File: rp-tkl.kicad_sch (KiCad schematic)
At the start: 33 parts, among them J1 USB_C_Receptacle_USB2.0, J2 SWD, SW0 SW_Push, U1 XC6206PxxxMR, U2 RP2040, U3 SRV05-4, U4 W25Q128JVS, Y1 12MHz

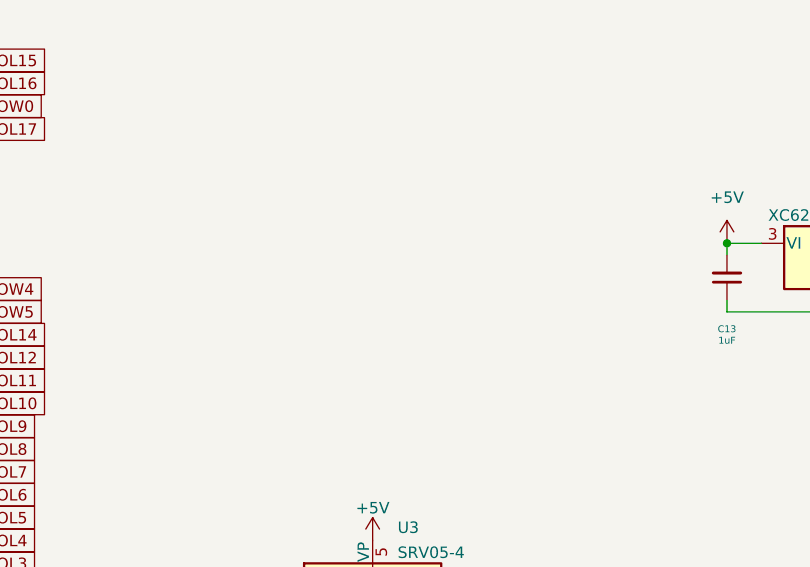
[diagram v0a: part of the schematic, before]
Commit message: Added JST Connector
Also cleaned up everything, 99% done
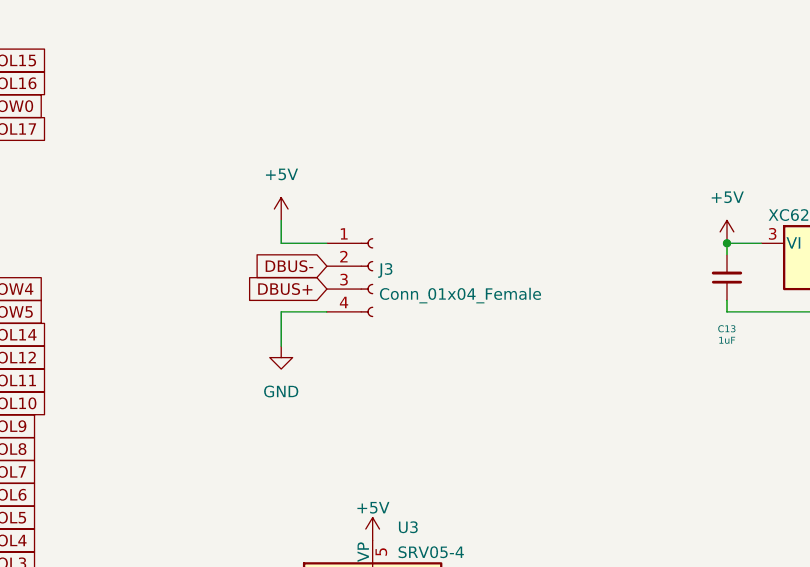
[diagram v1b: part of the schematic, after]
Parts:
- added J3: Conn_01x04_Female, Connector_JST:JST_SH_SM04B-SRSS-TB_1x04-1MP_P1.00mm_Horizontal, symbol Connector:Conn_01x04_Female
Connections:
- net +5V: now also J3.1 (Pin_1)
- net DBUS+: now also J3.3 (Pin_3)
- net DBUS-: now also J3.2 (Pin_2)
- net GND: now also J3.4 (Pin_4)
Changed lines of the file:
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@@
   (no_connect (at 72.39 199.39))
   (no_connect (at 72.39 201.93))
+  (wire (pts (xy 125.73 69.85) (xy 120.65 69.85))
+    (stroke (width 0) (type default) (color 0 0 0 0))
+  )
   (wire (pts (xy 87.63 171.45) (xy 92.71 171.45))
     (stroke (width 0) (type default) (color 0 0 0 0))
   )
+  (wire (pts (xy 125.73 77.47) (xy 120.65 77.47))
+    (stroke (width 0) (type default) (color 0 0 0 0))
+  )
   (wire (pts (xy 281.305 68.58) (xy 281.305 69.85))
     (stroke (width 0) (type default) (color 0 0 0 0))
@@
   )
   (wire (pts (xy 176.53 118.11) (xy 182.88 118.11))
+    (stroke (width 0) (type default) (color 0 0 0 0))
+  )
+  (wire (pts (xy 120.65 77.47) (xy 120.65 81.28))
     (stroke (width 0) (type default) (color 0 0 0 0))
   )
@@
   (wire (pts (xy 189.23 69.85) (xy 193.04 69.85))
     (stroke (width 0) (type solid) (color 0 0 0 0))
+  )
+  (wire (pts (xy 120.65 67.31) (xy 120.65 69.85))
+    (stroke (width 0) (type default) (color 0 0 0 0))
   )
   (wire (pts (xy 213.36 76.2) (xy 217.17 76.2))
@@
     )
   )
+  (global_label "DBUS+" (shape input) (at 125.73 74.93 180) (fields_autoplaced)
+    (effects (font (size 1.27 1.27)) (justify right))
+    (property "Intersheet References" "${INTERSHEET_REFS}" (id 0) (at 116.6645 74.8506 0)
+      (effects (font (size 1.27 1.27)) (justify right) hide)
+    )
+  )
   (global_label "DBUS-" (shape input) (at 143.51 118.11 0) (fields_autoplaced)
     (effects (font (size 1.27 1.27)) (justify left))
@@
     )
   )
+  (global_label "DBUS-" (shape input) (at 125.73 72.39 180) (fields_autoplaced)
+    (effects (font (size 1.27 1.27)) (justify right))
+    (property "Intersheet References" "${INTERSHEET_REFS}" (id 0) (at 116.6645 72.3106 0)
+      (effects (font (size 1.27 1.27)) (justify right) hide)
+    )
+  )
   (global_label "~{RESET}" (shape input) (at 240.03 111.76 0) (fields_autoplaced)
     (effects (font (size 1.27 1.27)) (justify left))
@@
     (pin "5")
     (pin "6")
+  )
+  (symbol (lib_id "power:GND") (at 120.65 81.28 0) (unit 1)
+    (in_bom yes) (on_board yes) (fields_autoplaced)
+    (property "Reference" "#PWR029" (id 0) (at 120.65 87.63 0)
+      (effects (font (size 1.27 1.27)) hide)
+    )
+    (property "Value" "GND" (id 1) (at 120.65 86.36 0))
+    (property "Footprint" "" (id 2) (at 120.65 81.28 0)
+      (effects (font (size 1.27 1.27)) hide)
+    )
+    (property "Datasheet" "" (id 3) (at 120.65 81.28 0)
+      (effects (font (size 1.27 1.27)) hide)
+    )
+    (pin "1")
   )
   (symbol (lib_id "Device:R_Small") (at 195.58 118.11 90) (unit 1)
@@
     (pin "1")
   )
+  (symbol (lib_id "power:+5V") (at 120.65 67.31 0) (unit 1)
+    (in_bom yes) (on_board yes) (fields_autoplaced)
+    (property "Reference" "#PWR0103" (id 0) (at 120.65 71.12 0)
+      (effects (font (size 1.27 1.27)) hide)
+    )
+    (property "Value" "+5V" (id 1) (at 120.65 62.23 0))
+    (property "Footprint" "" (id 2) (at 120.65 67.31 0)
+      (effects (font (size 1.27 1.27)) hide)
+    )
+    (property "Datasheet" "" (id 3) (at 120.65 67.31 0)
+      (effects (font (size 1.27 1.27)) hide)
+    )
+    (pin "1")
+  )
   (symbol (lib_id "Device:Crystal_GND24_Small") (at 182.88 115.57 90) (unit 1)
     (in_bom yes) (on_board yes)
@@
     (pin "1")
   )
+  (symbol (lib_id "Connector:Conn_01x04_Female") (at 130.81 72.39 0) (unit 1)
+    (in_bom yes) (on_board yes) (fields_autoplaced)
+    (property "Reference" "J3" (id 0) (at 131.5212 72.7515 0)
+      (effects (font (size 1.27 1.27)) (justify left))
+    )
+    (property "Value" "Conn_01x04_Female" (id 1) (at 131.5212 75.5266 0)
+      (effects (font (size 1.27 1.27)) (justify left))
+    )
+    (property "Footprint" "Connector_JST:JST_SH_SM04B-SRSS-TB_1x04-1MP_P1.00mm_Horizontal" (id 2) (at 130.81 72.39 0)
+      (effects (font (size 1.27 1.27)) hide)
+    )
+    (property "Datasheet" "~" (id 3) (at 130.81 72.39 0)
+      (effects (font (size 1.27 1.27)) hide)
+    )
+    (pin "1")
+    (pin "2")
+    (pin "3")
+    (pin "4")
+  )
   (symbol (lib_id "Device:C_Small") (at 222.25 72.39 0) (unit 1)
     (in_bom yes) (on_board yes)
@@
       (reference "#PWR027") (unit 1) (value "GND") (footprint "")
     )
+    (path "/40aa9167-fdb5-46eb-9a4f-8c98d55681c9"
+      (reference "#PWR029") (unit 1) (value "GND") (footprint "")
+    )
     (path "/13bc3998-5745-424e-ada9-f8a9e1f5329c"
       (reference "#PWR0101") (unit 1) (value "+3V3") (footprint "")
@@
       (reference "#PWR0102") (unit 1) (value "+1V1") (footprint "")
     )
+    (path "/79db240d-9612-4f89-9692-5a027e4d42fe"
+      (reference "#PWR0103") (unit 1) (value "+5V") (footprint "")
+    )
     (path "/29f11a32-f398-46d6-95a0-57f3be58392e"
       (reference "C1") (unit 1) (value "1uF") (footprint "Capacitor_SMD:C_0402_1005Metric")
@@
       (reference "J2") (unit 1) (value "SWD") (footprint "Connector_PinSocket_2.54mm:PinSocket_1x05_P2.54mm_Vertical")
     )
+    (path "/cd299587-3566-48c2-b7b0-ede206393480"
+      (reference "J3") (unit 1) (value "Conn_01x04_Female") (footprint "Connector_JST:JST_SH_SM04B-SRSS-TB_1x04-1MP_P1.00mm_Horizontal")
+    )
     (path "/d5f64c48-5769-4554-8a1d-d23f7b2152b1"

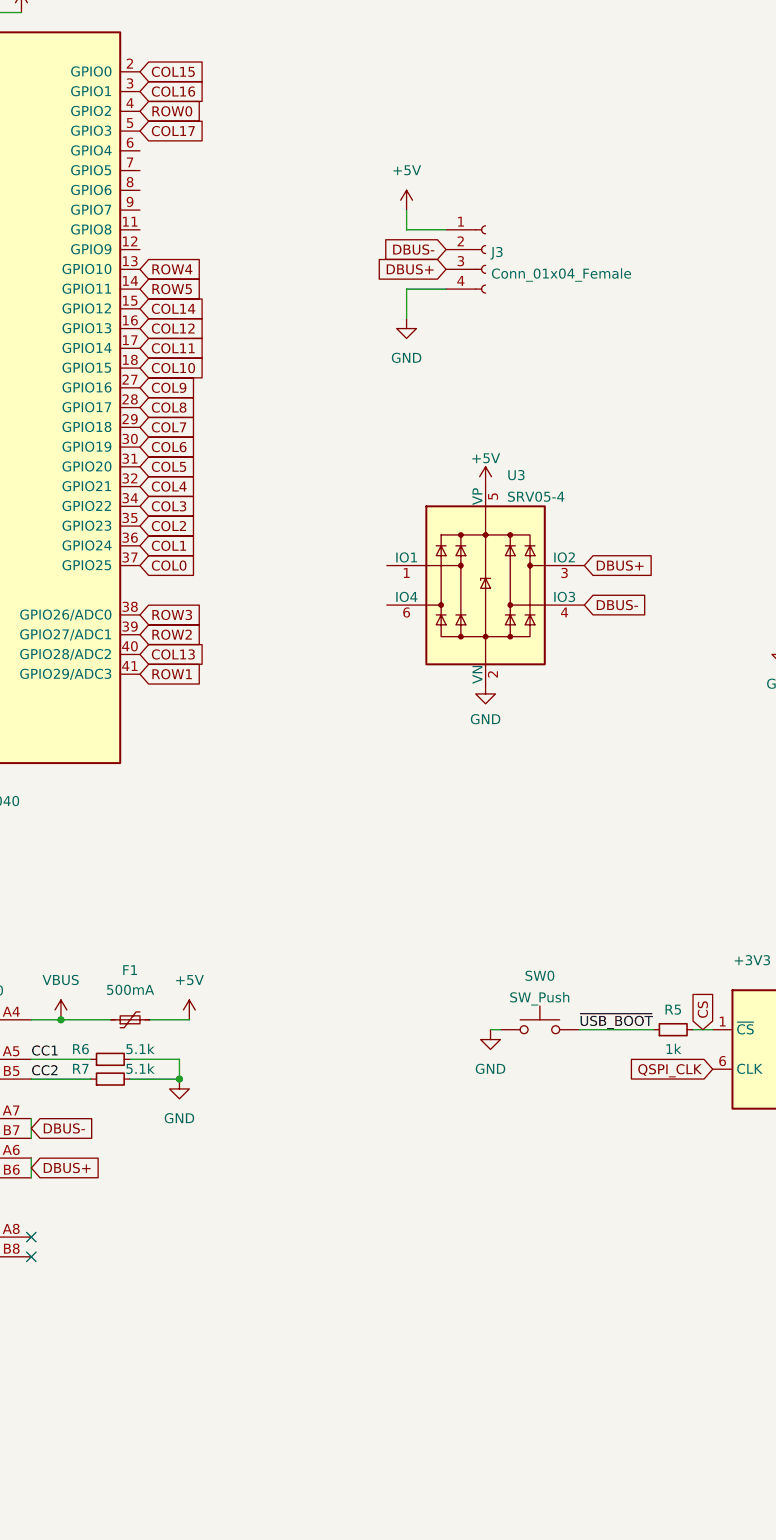
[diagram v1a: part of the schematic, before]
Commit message: More cleanup, added connector for/broke out unused pins
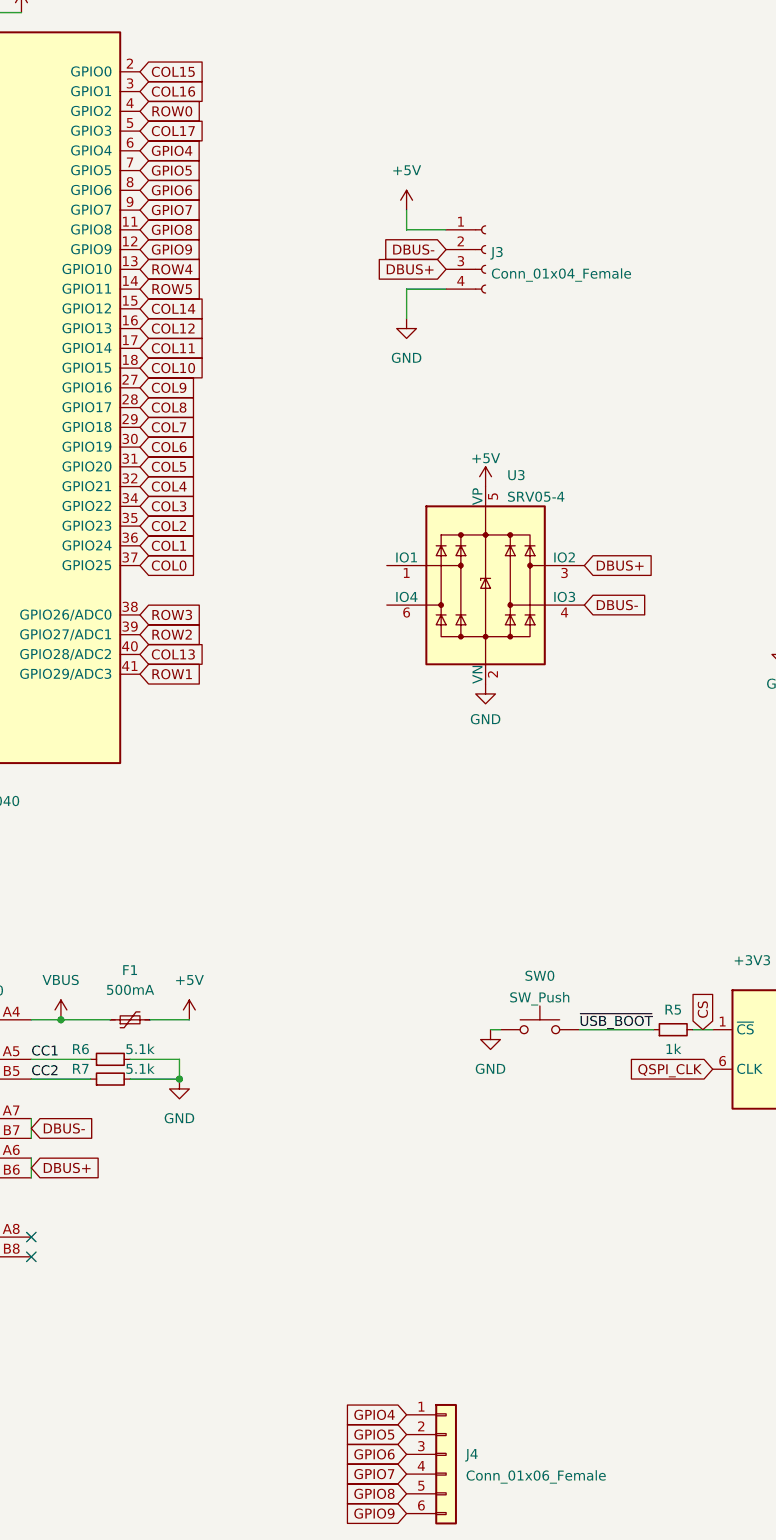
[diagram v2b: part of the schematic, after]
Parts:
- added J4: Conn_01x06_Female, Connector_PinSocket_2.54mm:PinSocket_1x06_P2.54mm_Vertical, symbol Connector_Generic:Conn_01x06
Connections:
- net GPIO8: now reaches U2.11 (GPIO8)
- net GPIO8: now also J4.5 (Pin_5)
- net GPIO9: now reaches U2.12 (GPIO9)
- net GPIO9: now also J4.6 (Pin_6)
- net GPIO4: now reaches U2.6 (GPIO4)
- net GPIO4: now also J4.1 (Pin_1)
- net GPIO5: now reaches U2.7 (GPIO5)
- net GPIO5: now also J4.2 (Pin_2)
- net GPIO6: now reaches U2.8 (GPIO6)
- net GPIO6: now also J4.3 (Pin_3)
- net GPIO7: now reaches U2.9 (GPIO7)
- net GPIO7: now also J4.4 (Pin_4)
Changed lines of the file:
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@@
+    )
+  )
+  (global_label "GPIO4" (shape input) (at 120.65 222.25 180) (fields_autoplaced)
+    (effects (font (size 1.27 1.27)) (justify right))
+    (property "Intersheet References" "${INTERSHEET_REFS}" (id 0) (at 112.5521 222.1706 0)
+      (effects (font (size 1.27 1.27)) (justify right) hide)
     )
   )
@@
     )
   )
+  (global_label "GPIO6" (shape input) (at 120.65 227.33 180) (fields_autoplaced)
+    (effects (font (size 1.27 1.27)) (justify right))
+    (property "Intersheet References" "${INTERSHEET_REFS}" (id 0) (at 112.5521 227.2506 0)
+      (effects (font (size 1.27 1.27)) (justify right) hide)
+    )
+  )
+  (global_label "GPIO7" (shape input) (at 120.65 229.87 180) (fields_autoplaced)
+    (effects (font (size 1.27 1.27)) (justify right))
+    (property "Intersheet References" "${INTERSHEET_REFS}" (id 0) (at 112.5521 229.7906 0)
+      (effects (font (size 1.27 1.27)) (justify right) hide)
+    )
+  )
   (global_label "COL12" (shape input) (at 86.36 82.55 0) (fields_autoplaced)
     (effects (font (size 1.27 1.27)) (justify left))
@@
     )
   )
+  (global_label "GPIO8" (shape input) (at 86.36 69.85 0) (fields_autoplaced)
+    (effects (font (size 1.27 1.27)) (justify left))
+    (property "Intersheet References" "${INTERSHEET_REFS}" (id 0) (at 94.4579 69.7706 0)
+      (effects (font (size 1.27 1.27)) (justify left) hide)
+    )
+  )
   (global_label "SD0" (shape input) (at 185.42 170.18 0) (fields_autoplaced)
     (effects (font (size 1.27 1.27)) (justify left))
@@
     )
   )
+  (global_label "GPIO9" (shape input) (at 120.65 234.95 180) (fields_autoplaced)
+    (effects (font (size 1.27 1.27)) (justify right))
+    (property "Intersheet References" "${INTERSHEET_REFS}" (id 0) (at 112.5521 234.8706 0)
+      (effects (font (size 1.27 1.27)) (justify right) hide)
+    )
+  )
+  (global_label "GPIO5" (shape input) (at 120.65 224.79 180) (fields_autoplaced)
+    (effects (font (size 1.27 1.27)) (justify right))
+    (property "Intersheet References" "${INTERSHEET_REFS}" (id 0) (at 112.5521 224.7106 0)
+      (effects (font (size 1.27 1.27)) (justify right) hide)
+    )
+  )
   (global_label "COL0" (shape input) (at 86.36 113.03 0) (fields_autoplaced)
     (effects (font (size 1.27 1.27)) (justify left))
@@
     )
   )
+  (global_label "GPIO4" (shape input) (at 86.36 59.69 0) (fields_autoplaced)
+    (effects (font (size 1.27 1.27)) (justify left))
+    (property "Intersheet References" "${INTERSHEET_REFS}" (id 0) (at 94.4579 59.6106 0)
+      (effects (font (size 1.27 1.27)) (justify left) hide)
+    )
+  )
   (global_label "SD2" (shape input) (at 45.72 121.92 180) (fields_autoplaced)
     (effects (font (size 1.27 1.27)) (justify right))
@@
     )
   )
+  (global_label "GPIO5" (shape input) (at 86.36 62.23 0) (fields_autoplaced)
+    (effects (font (size 1.27 1.27)) (justify left))
+    (property "Intersheet References" "${INTERSHEET_REFS}" (id 0) (at 94.4579 62.1506 0)
+      (effects (font (size 1.27 1.27)) (justify left) hide)
+    )
+  )
   (global_label "COL3" (shape input) (at 86.36 105.41 0) (fields_autoplaced)
     (effects (font (size 1.27 1.27)) (justify left))
@@
     )
   )
+  (global_label "GPIO6" (shape input) (at 86.36 64.77 0) (fields_autoplaced)
+    (effects (font (size 1.27 1.27)) (justify left))
+    (property "Intersheet References" "${INTERSHEET_REFS}" (id 0) (at 94.4579 64.6906 0)
+      (effects (font (size 1.27 1.27)) (justify left) hide)
+    )
+  )
   (global_label "SD1" (shape input) (at 185.42 172.72 0) (fields_autoplaced)
     (effects (font (size 1.27 1.27)) (justify left))
@@
     (property "Intersheet References" "${INTERSHEET_REFS}" (id 0) (at 94.0345 119.3006 0)
       (effects (font (size 1.27 1.27)) (justify left) hide)
+    )
+  )
+  (global_label "GPIO8" (shape input) (at 120.65 232.41 180) (fields_autoplaced)
+    (effects (font (size 1.27 1.27)) (justify right))
+    (property "Intersheet References" "${INTERSHEET_REFS}" (id 0) (at 112.5521 232.3306 0)
+      (effects (font (size 1.27 1.27)) (justify right) hide)
     )
   )
@@
     )
   )
+  (global_label "GPIO9" (shape input) (at 86.36 72.39 0) (fields_autoplaced)
+    (effects (font (size 1.27 1.27)) (justify left))
+    (property "Intersheet References" "${INTERSHEET_REFS}" (id 0) (at 94.4579 72.3106 0)
+      (effects (font (size 1.27 1.27)) (justify left) hide)
+    )
+  )
   (global_label "XTAL_OUT" (shape input) (at 45.72 78.74 180) (fields_autoplaced)
     (effects (font (size 1.27 1.27)) (justify right))
@@
     (effects (font (size 1.27 1.27)) (justify left))
     (property "Intersheet References" "${INTERSHEET_REFS}" (id 0) (at 191.5221 177.7206 0)
+      (effects (font (size 1.27 1.27)) (justify left) hide)
+    )
+  )
+  (global_label "GPIO7" (shape input) (at 86.36 67.31 0) (fields_autoplaced)
+    (effects (font (size 1.27 1.27)) (justify left))
+    (property "Intersheet References" "${INTERSHEET_REFS}" (id 0) (at 94.4579 67.2306 0)
       (effects (font (size 1.27 1.27)) (justify left) hide)
     )
@@
     (pin "1")
   )
+  (symbol (lib_id "Connector_Generic:Conn_01x06") (at 125.73 227.33 0) (unit 1)
+    (in_bom yes) (on_board yes)
+    (property "Reference" "J4" (id 0) (at 128.27 227.33 0)
+      (effects (font (size 1.27 1.27)) (justify left))
+    )
+    (property "Value" "Conn_01x06_Female" (id 1) (at 128.27 230.1051 0)
+      (effects (font (size 1.27 1.27)) (justify left))
+    )
+    (property "Footprint" "Connector_PinSocket_2.54mm:PinSocket_1x06_P2.54mm_Vertical" (id 2) (at 125.73 227.33 0)
+      (effects (font (size 1.27 1.27)) hide)
+    )
+    (property "Datasheet" "~" (id 3) (at 125.73 227.33 0)
+      (effects (font (size 1.27 1.27)) hide)
+    )
+    (pin "1")
+    (pin "2")
+    (pin "3")
+    (pin "4")
+    (pin "5")
+    (pin "6")
+  )
   (symbol (lib_id "Device:Crystal_GND24_Small") (at 182.88 115.57 90) (unit 1)
     (in_bom yes) (on_board yes)
@@
       (reference "J3") (unit 1) (value "Conn_01x04_Female") (footprint "Connector_JST:JST_SH_SM04B-SRSS-TB_1x04-1MP_P1.00mm_Horizontal")
     )
+    (path "/7e5da8d0-bec9-4daa-a9a1-871fdaa0d15e"
+      (reference "J4") (unit 1) (value "Conn_01x06_Female") (footprint "Connector_PinSocket_2.54mm:PinSocket_1x06_P2.54mm_Vertical")
+    )
     (path "/d5f64c48-5769-4554-8a1d-d23f7b2152b1"
